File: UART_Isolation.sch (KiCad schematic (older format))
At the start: 8 parts

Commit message: Updated UART USB converter sheet, and isolation sheet
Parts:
- removed R905: 10k, Resistors_SMD:R_0603, symbol Custom-Library:R_Custom
- added U901: ISO7331C, Package_SO:SOIC-16W_7.5x10.3mm_P1.27mm, symbol Isolator:ISO7331C
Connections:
- net labels added: USB_DTR, USB_DTR_ISO
- net labels removed: ~USB_DTR, ~USB_DTR_ISO
- wire segments 34 -> 32
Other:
- note removed: "SWITCH TO DUAL SIGNAL ISOLATOR INSTEAD"
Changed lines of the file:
@@
 USB_UART_RX_ISO
 Text GLabel 7300 3700 2    60   Input ~ 0
-~USB_DTR_ISO
+USB_DTR_ISO
 $Comp
 L Custom-Library:GND_USB #PWR908
@@
 	4810 3900 4890 3900
 Connection ~ 4810 4000
-$Comp
-L Custom-Library:R_Custom R905
-U 1 1 5B330ED8
-P 6530 2940
-F 0 "R905" H 6470 2940 50  0000 R CNN
-F 1 "10k" V 6530 2940 50  0000 C CNN
-F 2 "Resistors_SMD:R_0603" H 6530 2940 50  0001 C CNN
-F 3 "" H 6530 2940 50  0001 C CNN
-F 4 "0603" H 6600 3020 50  0000 L CNN "display_footprint"
-F 5 "1%" H 6600 2940 50  0000 L CNN "Tolerance"
-F 6 "1/10W" H 6600 2870 50  0000 L CNN "Wattage"
-	1    6530 2940
-	1    0    0    1
-$EndComp
 Wire Wire Line
 	5690 3600 6220 3600
-Wire Wire Line
-	5690 3700 6530 3700
 Wire Wire Line
 	5690 3800 6860 3800
@@
 $EndComp
 Wire Wire Line
-	6530 3090 6530 3700
-Connection ~ 6530 3700
-Wire Wire Line
 	6860 3900 6860 3800
 Connection ~ 6860 3800
@@
 	1    0    0    -1
 $EndComp
-$Comp
-L Custom-Library:+5V_USB #PWR913
-U 1 1 5B334AE5
-P 6530 2790
-F 0 "#PWR913" H 6530 2640 50  0001 C CNN
-F 1 "+5V_USB" H 6530 2930 50  0000 C CNN
-F 2 "" H 6530 2790 50  0001 C CNN
-F 3 "" H 6530 2790 50  0001 C CNN
-	1    6530 2790
-	1    0    0    -1
-$EndComp
 Text GLabel 3280 3800 0    60   Input ~ 0
 USB_UART_TX
@@
 USB_UART_RX
 Text GLabel 3280 3700 0    60   Output ~ 0
-~USB_DTR
+USB_DTR
 $Comp
 L Custom-Library:R_Custom R902
@@
 	4810 4000 4810 4080
 Wire Wire Line
-	6530 3700 7300 3700
-Wire Wire Line
 	6860 3800 7300 3800
 Wire Wire Line
@@
 Wire Wire Line
 	4360 3600 4890 3600
-Text Notes 4480 1990 0    60   ~ 0
-SWITCH TO DUAL SIGNAL ISOLATOR INSTEAD
+Wire Wire Line
+	5690 3700 7300 3700
+$Comp
+L Isolator:ISO7331C U901
+U 1 1 5B50F39B
+P 5290 3700
+F 0 "U901" H 5040 4150 50  0000 C CNN
+F 1 "ISO7331C" H 5560 4150 50  0000 C CNN
+F 2 "Package_SO:SOIC-16W_7.5x10.3mm_P1.27mm" H 5290 3200 50  0001 C CIN
+F 3 "http://www.ti.com/lit/ds/symlink/iso7331c.pdf" H 5290 4100 50  0001 C CNN
+	1    5290 3700
+	-1   0    0    -1
+$EndComp
 $EndSCHEMATC

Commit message: Added a config field for every part, DNP some I2C pullups, added I2C header, changed some serial port functionality
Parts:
- removed R902: 10k, Resistors_SMD:R_0603, symbol Custom-Library:R_Custom
- added R? (x2): 10k, Resistors_SMD:R_0603, symbol Custom-Library:R_Custom
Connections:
- wire segments 32 -> 34
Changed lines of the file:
@@
 Comment4 ""
 $EndDescr
-Text GLabel 7300 3800 2    60   Output ~ 0
+Text GLabel 8000 3800 2    60   Output ~ 0
 USB_UART_TX_ISO
-Text GLabel 7300 3600 2    60   Input ~ 0
+Text GLabel 8000 3600 2    60   Input ~ 0
 USB_UART_RX_ISO
-Text GLabel 7300 3700 2    60   Input ~ 0
+Text GLabel 8000 3700 2    60   Input ~ 0
 USB_DTR_ISO
 $Comp
@@
 	1    0    0    -1
 $EndComp
-Text GLabel 3280 3800 0    60   Input ~ 0
+Text GLabel 2580 3800 0    60   Input ~ 0
 USB_UART_TX
-Text GLabel 3280 3600 0    60   Output ~ 0
+Text GLabel 2580 3600 0    60   Output ~ 0
 USB_UART_RX
-Text GLabel 3280 3700 0    60   Output ~ 0
+Text GLabel 2580 3700 0    60   Output ~ 0
 USB_DTR
-$Comp
-L Custom-Library:R_Custom R902
-U 1 1 5B334B6B
-P 4050 2940
-F 0 "R902" H 3990 2940 50  0000 R CNN
-F 1 "10k" V 4050 2940 50  0000 C CNN
-F 2 "Resistors_SMD:R_0603" H 4050 2940 50  0001 C CNN
-F 3 "" H 4050 2940 50  0001 C CNN
-F 4 "0603" H 4120 3020 50  0000 L CNN "display_footprint"
-F 5 "1%" H 4120 2940 50  0000 L CNN "Tolerance"
-F 6 "1/10W" H 4120 2870 50  0000 L CNN "Wattage"
-	1    4050 2940
-	-1   0    0    1
-$EndComp
-Wire Wire Line
-	3280 3600 4360 3600
-Wire Wire Line
-	3280 3700 4050 3700
-Wire Wire Line
-	3280 3800 3720 3800
 $Comp
 L Custom-Library:R_Custom R903
@@
 $EndComp
 Wire Wire Line
-	4050 3090 4050 3700
-Connection ~ 4050 3700
-Wire Wire Line
 	3720 3900 3720 3800
 Connection ~ 3720 3800
@@
 	4360 3900 4360 3600
 Connection ~ 4360 3600
-$Comp
-L Custom-Library:+3.3V #PWR902
-U 1 1 5B334D0F
-P 4050 2790
-F 0 "#PWR902" H 4050 2640 50  0001 C CNN
-F 1 "+3.3V" H 4050 2930 50  0000 C CNN
-F 2 "" H 4050 2790 50  0000 C CNN
-F 3 "" H 4050 2790 50  0000 C CNN
-	1    4050 2790
-	1    0    0    -1
-$EndComp
 $Comp
 L power:GND #PWR903
@@
 	4810 4000 4810 4080
 Wire Wire Line
-	6860 3800 7300 3800
-Wire Wire Line
-	6220 3600 7300 3600
-Wire Wire Line
 	6000 3400 6000 3500
 Wire Wire Line
 	4660 3400 4660 3500
 Wire Wire Line
-	4050 3700 4890 3700
-Wire Wire Line
 	3720 3800 4890 3800
 Wire Wire Line
 	4360 3600 4890 3600
-Wire Wire Line
-	5690 3700 7300 3700
 $Comp
 L Isolator:ISO7331C U901
@@
 	-1   0    0    -1
 $EndComp
+Wire Wire Line
+	6220 3600 8000 3600
+Wire Wire Line
+	6860 3800 8000 3800
+Wire Wire Line
+	5690 3700 7530 3700
+Wire Wire Line
+	2580 3600 4360 3600
+$Comp
+L Custom-Library:R_Custom R?
+U 1 1 5B51D46D
+P 3110 4050
+F 0 "R?" H 3050 4050 50  0000 R CNN
+F 1 "10k" V 3110 4050 50  0000 C CNN
+F 2 "Resistors_SMD:R_0603" H 3110 4050 50  0001 C CNN
+F 3 "" H 3110 4050 50  0001 C CNN
+F 4 "0603" H 3180 4130 50  0000 L CNN "display_footprint"
+F 5 "1%" H 3180 4050 50  0000 L CNN "Tolerance"
+F 6 "1/10W" H 3180 3980 50  0000 L CNN "Wattage"
+	1    3110 4050
+	-1   0    0    1
+$EndComp
+$Comp
+L power:GND #PWR?
+U 1 1 5B51D49E
+P 3110 4200
+F 0 "#PWR?" H 3110 3950 50  0001 C CNN
+F 1 "GND" H 3110 4050 50  0000 C CNN
+F 2 "" H 3110 4200 50  0001 C CNN
+F 3 "" H 3110 4200 50  0001 C CNN
+	1    3110 4200
+	1    0    0    -1
+$EndComp
+Wire Wire Line
+	3110 3900 3110 3700
+Wire Wire Line
+	2580 3800 3720 3800
+Wire Wire Line
+	2580 3700 3110 3700
+Connection ~ 3110 3700
+Wire Wire Line
+	3110 3700 4890 3700
+$Comp
+L Custom-Library:R_Custom R?
+U 1 1 5B51DA55
+P 7530 4050
+F 0 "R?" H 7470 4050 50  0000 R CNN
+F 1 "10k" V 7530 4050 50  0000 C CNN
+F 2 "Resistors_SMD:R_0603" H 7530 4050 50  0001 C CNN
+F 3 "" H 7530 4050 50  0001 C CNN
+F 4 "0603" H 7600 4130 50  0000 L CNN "display_footprint"
+F 5 "1%" H 7600 4050 50  0000 L CNN "Tolerance"
+F 6 "1/10W" H 7600 3980 50  0000 L CNN "Wattage"
+	1    7530 4050
+	1    0    0    1
+$EndComp
+$Comp
+L Custom-Library:GND_USB #PWR?
+U 1 1 5B51DA86
+P 7530 4200
+F 0 "#PWR?" H 7530 3950 50  0001 C CNN
+F 1 "GND_USB" H 7530 4050 50  0000 C CNN
+F 2 "" H 7530 4200 50  0001 C CNN
+F 3 "" H 7530 4200 50  0001 C CNN
+	1    7530 4200
+	1    0    0    -1
+$EndComp
+Wire Wire Line
+	7530 3900 7530 3700
+Connection ~ 7530 3700
+Wire Wire Line
+	7530 3700 8000 3700
 $EndSCHEMATC

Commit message: Annotated all components, finished assigning footprints, netlist generated
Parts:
- gave numbers to parts that had none: 2
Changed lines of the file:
@@
 USB_DTR_ISO
 $Comp
-L Custom-Library:GND_USB #PWR908
+L Custom-Library:GND_USB #PWR0908
 U 1 1 5B33B4C2
 P 5770 4080
-F 0 "#PWR908" H 5770 3830 50  0001 C CNN
+F 0 "#PWR0908" H 5770 3830 50  0001 C CNN
 F 1 "GND_USB" H 5770 3930 50  0000 C CNN
 F 2 "" H 5770 4080 50  0001 C CNN
@@
 Connection ~ 5770 4000
 $Comp
-L power:GND #PWR905
+L power:GND #PWR0905
 U 1 1 5B33B4E7
 P 4810 4080
-F 0 "#PWR905" H 4810 3830 50  0001 C CNN
+F 0 "#PWR0905" H 4810 3830 50  0001 C CNN
 F 1 "GND" H 4810 3930 50  0000 C CNN
 F 2 "" H 4810 4080 50  0001 C CNN
@@
 $EndComp
 $Comp
-L Custom-Library:GND_USB #PWR912
+L Custom-Library:GND_USB #PWR0912
 U 1 1 5B3334DB
 P 6220 4200
-F 0 "#PWR912" H 6220 3950 50  0001 C CNN
+F 0 "#PWR0912" H 6220 3950 50  0001 C CNN
 F 1 "GND_USB" H 6220 4050 50  0000 C CNN
 F 2 "" H 6220 4200 50  0001 C CNN
@@
 $EndComp
 $Comp
-L Custom-Library:GND_USB #PWR914
+L Custom-Library:GND_USB #PWR0914
 U 1 1 5B3334F2
 P 6860 4200
-F 0 "#PWR914" H 6860 3950 50  0001 C CNN
+F 0 "#PWR0914" H 6860 3950 50  0001 C CNN
 F 1 "GND_USB" H 6860 4050 50  0000 C CNN
 F 2 "" H 6860 4200 50  0001 C CNN
@@
 $EndComp
 $Comp
-L power:GND #PWR907
+L power:GND #PWR0907
 U 1 1 5B333B49
 P 4830 4900
-F 0 "#PWR907" H 4830 4650 50  0001 C CNN
+F 0 "#PWR0907" H 4830 4650 50  0001 C CNN
 F 1 "GND" H 4830 4750 50  0000 C CNN
 F 2 "" H 4830 4900 50  0001 C CNN
@@
 $EndComp
 $Comp
-L Custom-Library:GND_USB #PWR910
+L Custom-Library:GND_USB #PWR0910
 U 1 1 5B333B66
 P 5940 4900
-F 0 "#PWR910" H 5940 4650 50  0001 C CNN
+F 0 "#PWR0910" H 5940 4650 50  0001 C CNN
 F 1 "GND_USB" H 5940 4750 50  0000 C CNN
 F 2 "" H 5940 4900 50  0001 C CNN
@@
 $EndComp
 $Comp
-L Custom-Library:+5V_USB #PWR911
+L Custom-Library:+5V_USB #PWR0911
 U 1 1 5B333B91
 P 6000 3320
-F 0 "#PWR911" H 6000 3170 50  0001 C CNN
+F 0 "#PWR0911" H 6000 3170 50  0001 C CNN
 F 1 "+5V_USB" H 6000 3460 50  0000 C CNN
 F 2 "" H 6000 3320 50  0001 C CNN
@@
 Connection ~ 6000 3400
 $Comp
-L Custom-Library:+3.3V #PWR904
+L Custom-Library:+3.3V #PWR0904
 U 1 1 5B334082
 P 4660 3320
-F 0 "#PWR904" H 4660 3170 50  0001 C CNN
+F 0 "#PWR0904" H 4660 3170 50  0001 C CNN
 F 1 "+3.3V" H 4660 3460 50  0000 C CNN
 F 2 "" H 4660 3320 50  0000 C CNN
@@
 Connection ~ 4660 3400
 $Comp
-L Custom-Library:+5V_USB #PWR909
+L Custom-Library:+5V_USB #PWR0909
 U 1 1 5B33458B
 P 5940 4600
-F 0 "#PWR909" H 5940 4450 50  0001 C CNN
+F 0 "#PWR0909" H 5940 4450 50  0001 C CNN
 F 1 "+5V_USB" H 5940 4740 50  0000 C CNN
 F 2 "" H 5940 4600 50  0001 C CNN
@@
 $EndComp
 $Comp
-L Custom-Library:+3.3V #PWR906
+L Custom-Library:+3.3V #PWR0906
 U 1 1 5B3345D2
 P 4830 4600
-F 0 "#PWR906" H 4830 4450 50  0001 C CNN
+F 0 "#PWR0906" H 4830 4450 50  0001 C CNN
 F 1 "+3.3V" H 4830 4740 50  0000 C CNN
 F 2 "" H 4830 4600 50  0000 C CNN
@@
 Connection ~ 4360 3600
 $Comp
-L power:GND #PWR903
+L power:GND #PWR0903
 U 1 1 5B334D88
 P 4360 4200
-F 0 "#PWR903" H 4360 3950 50  0001 C CNN
+F 0 "#PWR0903" H 4360 3950 50  0001 C CNN
 F 1 "GND" H 4360 4050 50  0000 C CNN
 F 2 "" H 4360 4200 50  0001 C CNN
@@
 $EndComp
 $Comp
-L power:GND #PWR901
+L power:GND #PWR0901
 U 1 1 5B33526C
 P 3720 4200
-F 0 "#PWR901" H 3720 3950 50  0001 C CNN
+F 0 "#PWR0901" H 3720 3950 50  0001 C CNN
 F 1 "GND" H 3720 4050 50  0000 C CNN
 F 2 "" H 3720 4200 50  0001 C CNN
@@
 	2580 3600 4360 3600
 $Comp
-L Custom-Library:R_Custom R?
+L Custom-Library:R_Custom R902
 U 1 1 5B51D46D
 P 3110 4050
-F 0 "R?" H 3050 4050 50  0000 R CNN
+F 0 "R902" H 3050 4050 50  0000 R CNN
 F 1 "10k" V 3110 4050 50  0000 C CNN
 F 2 "Resistors_SMD:R_0603" H 3110 4050 50  0001 C CNN
@@
 $EndComp
 $Comp
-L power:GND #PWR?
+L power:GND #PWR0902
 U 1 1 5B51D49E
 P 3110 4200
-F 0 "#PWR?" H 3110 3950 50  0001 C CNN
+F 0 "#PWR0902" H 3110 3950 50  0001 C CNN
 F 1 "GND" H 3110 4050 50  0000 C CNN
 F 2 "" H 3110 4200 50  0001 C CNN
@@
 	3110 3700 4890 3700
 $Comp
-L Custom-Library:R_Custom R?
+L Custom-Library:R_Custom R905
 U 1 1 5B51DA55
 P 7530 4050
-F 0 "R?" H 7470 4050 50  0000 R CNN
+F 0 "R905" H 7470 4050 50  0000 R CNN
 F 1 "10k" V 7530 4050 50  0000 C CNN
 F 2 "Resistors_SMD:R_0603" H 7530 4050 50  0001 C CNN
@@
 $EndComp
 $Comp
-L Custom-Library:GND_USB #PWR?
+L Custom-Library:GND_USB #PWR0913
 U 1 1 5B51DA86
 P 7530 4200
-F 0 "#PWR?" H 7530 3950 50  0001 C CNN
+F 0 "#PWR0913" H 7530 3950 50  0001 C CNN
 F 1 "GND_USB" H 7530 4050 50  0000 C CNN
 F 2 "" H 7530 4200 50  0001 C CNN

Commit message: Changed POS3P3 MOSFETs, further schematic enhancements, footprint updates, and arranged a few more pages of components on PCB
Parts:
- U901: footprint Package_SO:SOIC-16W_7.5x10.3mm_P1.27mm -> Housings_SOIC:SOIC-16W_7.5x10.3mm_Pitch1.27mm; Digi-Key PN (none) -> 296-47261-1-ND
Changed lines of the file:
@@
 F 0 "U901" H 5040 4150 50  0000 C CNN
 F 1 "ISO7331C" H 5560 4150 50  0000 C CNN
-F 2 "Package_SO:SOIC-16W_7.5x10.3mm_P1.27mm" H 5290 3200 50  0001 C CIN
+F 2 "Housings_SOIC:SOIC-16W_7.5x10.3mm_Pitch1.27mm" H 5290 3200 50  0001 C CIN
 F 3 "http://www.ti.com/lit/ds/symlink/iso7331c.pdf" H 5290 4100 50  0001 C CNN
+F 4 "296-47261-1-ND" H 5290 3700 50  0001 C CNN "Digi-Key PN"
 	1    5290 3700
 	-1   0    0    -1

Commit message: Arranged USB components, various footprint fixes, added GND_USB EMI cap
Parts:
- added C903: 22000pF, Capacitors_SMD:C_2220, symbol Custom-Library:C_Custom
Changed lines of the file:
@@
 Wire Wire Line
 	7530 3700 8000 3700
+$Comp
+L Custom-Library:C_Custom C?
+U 1 1 5B585E45
+P 5290 5320
+AR Path="/5A0A3EA5/5B585E45" Ref="C?"  Part="1"
+AR Path="/5A0B00BA/5B585E45" Ref="C?"  Part="1"
+AR Path="/5A19B2DB/5B585E45" Ref="C903"  Part="1"
+F 0 "C903" V 5450 5320 50  0000 C CNN
+F 1 "22000pF" V 5541 5320 50  0000 C CNN
+F 2 "Capacitors_SMD:C_2220" H 5328 5170 50  0001 C CNN
+F 3 "" H 5315 5420 50  0001 C CNN
+F 4 "2220" V 5632 5320 50  0000 C CNN "display_footprint"
+F 5 "250VAC" V 5723 5320 50  0000 C CNN "Voltage"
+F 6 "X7R" V 5814 5320 50  0000 C CNN "Dielectric"
+F 7 "720-1587-1-ND" V 5290 5320 50  0001 C CNN "Digi-Key PN"
+	1    5290 5320
+	0    1    1    0
+$EndComp
+$Comp
+L Custom-Library:GND_USB #PWR0103
+U 1 1 5B58639E
+P 5440 5320
+F 0 "#PWR0103" H 5440 5070 50  0001 C CNN
+F 1 "GND_USB" H 5440 5170 50  0000 C CNN
+F 2 "" H 5440 5320 50  0001 C CNN
+F 3 "" H 5440 5320 50  0001 C CNN
+	1    5440 5320
+	0    -1   -1   0
+$EndComp
+$Comp
+L power:GND #PWR0104
+U 1 1 5B5863DB
+P 5140 5320
+F 0 "#PWR0104" H 5140 5070 50  0001 C CNN
+F 1 "GND" H 5140 5170 50  0000 C CNN
+F 2 "" H 5140 5320 50  0001 C CNN
+F 3 "" H 5140 5320 50  0001 C CNN
+	1    5140 5320
+	0    1    1    0
+$EndComp
 $EndSCHEMATC

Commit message: Added a bunch of Digi-Key PN's
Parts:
- C901, C902: Digi-Key PN (none) -> 399-6856-1-ND
- R901, R902, R903, R904, R905, R906: Digi-Key PN (none) -> 541-10.0KHCT-ND
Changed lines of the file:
@@
 F 5 "1%" H 6290 4050 50  0000 L CNN "Tolerance"
 F 6 "1/10W" H 6290 3980 50  0000 L CNN "Wattage"
+F 7 "541-10.0KHCT-ND" H 0   0   50  0001 C CNN "Digi-Key PN"
 	1    6220 4050
 	1    0    0    1
@@
 F 5 "1%" H 6930 4050 50  0000 L CNN "Tolerance"
 F 6 "1/10W" H 6930 3980 50  0000 L CNN "Wattage"
+F 7 "541-10.0KHCT-ND" H 0   0   50  0001 C CNN "Digi-Key PN"
 	1    6860 4050
 	1    0    0    1
@@
 F 5 "50V" H 5790 4750 50  0000 R CNN "Voltage"
 F 6 "X7R" H 5790 4650 50  0000 R CNN "Dielectric"
+F 7 "399-6856-1-ND" H 0   0   50  0001 C CNN "Digi-Key PN"
 	1    5940 4750
 	1    0    0    -1
@@
 F 5 "50V" H 4680 4750 50  0000 R CNN "Voltage"
 F 6 "X7R" H 4680 4650 50  0000 R CNN "Dielectric"
+F 7 "399-6856-1-ND" H 0   0   50  0001 C CNN "Digi-Key PN"
 	1    4830 4750
 	1    0    0    -1
@@
 F 5 "1%" H 4430 4050 50  0000 L CNN "Tolerance"
 F 6 "1/10W" H 4430 3980 50  0000 L CNN "Wattage"
+F 7 "541-10.0KHCT-ND" H 0   0   50  0001 C CNN "Digi-Key PN"
 	1    4360 4050
 	-1   0    0    1
@@
 F 5 "1%" H 3790 4050 50  0000 L CNN "Tolerance"
 F 6 "1/10W" H 3790 3980 50  0000 L CNN "Wattage"
+F 7 "541-10.0KHCT-ND" H 0   0   50  0001 C CNN "Digi-Key PN"
 	1    3720 4050
 	-1   0    0    1
@@
 F 5 "1%" H 3180 4050 50  0000 L CNN "Tolerance"
 F 6 "1/10W" H 3180 3980 50  0000 L CNN "Wattage"
+F 7 "541-10.0KHCT-ND" H 0   0   50  0001 C CNN "Digi-Key PN"
 	1    3110 4050
 	-1   0    0    1
@@
 F 5 "1%" H 7600 4050 50  0000 L CNN "Tolerance"
 F 6 "1/10W" H 7600 3980 50  0000 L CNN "Wattage"
+F 7 "541-10.0KHCT-ND" H 0   0   50  0001 C CNN "Digi-Key PN"
 	1    7530 4050
 	1    0    0    1

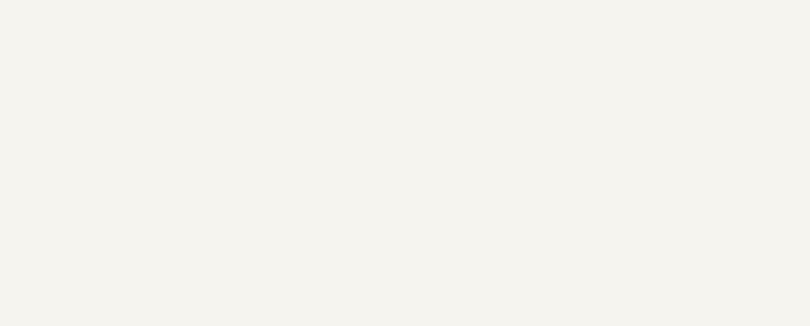
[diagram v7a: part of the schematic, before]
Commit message: Arranged more components on PCB, cleaned up schematic, added page titles, finished finding DigiKey PN's
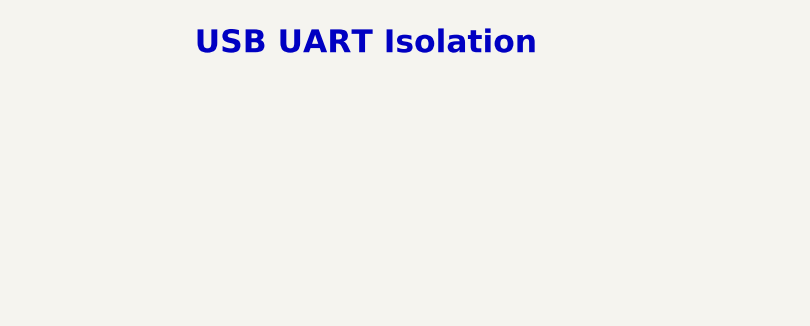
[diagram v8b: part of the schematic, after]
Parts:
- R901, R902, R903, R904, R905, R906: Digi-Key PN 541-10.0KHCT-ND -> P10.0KHCT-ND
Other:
- note added: "USB UART Isolation"
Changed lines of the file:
@@
 F 5 "1%" H 6290 4050 50  0000 L CNN "Tolerance"
 F 6 "1/10W" H 6290 3980 50  0000 L CNN "Wattage"
-F 7 "541-10.0KHCT-ND" H 0   0   50  0001 C CNN "Digi-Key PN"
+F 7 "P10.0KHCT-ND" H 0   0   50  0001 C CNN "Digi-Key PN"
 	1    6220 4050
 	1    0    0    1
@@
 F 5 "1%" H 6930 4050 50  0000 L CNN "Tolerance"
 F 6 "1/10W" H 6930 3980 50  0000 L CNN "Wattage"
-F 7 "541-10.0KHCT-ND" H 0   0   50  0001 C CNN "Digi-Key PN"
+F 7 "P10.0KHCT-ND" H 0   0   50  0001 C CNN "Digi-Key PN"
 	1    6860 4050
 	1    0    0    1
@@
 F 5 "1%" H 4430 4050 50  0000 L CNN "Tolerance"
 F 6 "1/10W" H 4430 3980 50  0000 L CNN "Wattage"
-F 7 "541-10.0KHCT-ND" H 0   0   50  0001 C CNN "Digi-Key PN"
+F 7 "P10.0KHCT-ND" H 0   0   50  0001 C CNN "Digi-Key PN"
 	1    4360 4050
 	-1   0    0    1
@@
 F 5 "1%" H 3790 4050 50  0000 L CNN "Tolerance"
 F 6 "1/10W" H 3790 3980 50  0000 L CNN "Wattage"
-F 7 "541-10.0KHCT-ND" H 0   0   50  0001 C CNN "Digi-Key PN"
+F 7 "P10.0KHCT-ND" H 0   0   50  0001 C CNN "Digi-Key PN"
 	1    3720 4050
 	-1   0    0    1
@@
 F 5 "1%" H 3180 4050 50  0000 L CNN "Tolerance"
 F 6 "1/10W" H 3180 3980 50  0000 L CNN "Wattage"
-F 7 "541-10.0KHCT-ND" H 0   0   50  0001 C CNN "Digi-Key PN"
+F 7 "P10.0KHCT-ND" H 0   0   50  0001 C CNN "Digi-Key PN"
 	1    3110 4050
 	-1   0    0    1
@@
 F 5 "1%" H 7600 4050 50  0000 L CNN "Tolerance"
 F 6 "1/10W" H 7600 3980 50  0000 L CNN "Wattage"
-F 7 "541-10.0KHCT-ND" H 0   0   50  0001 C CNN "Digi-Key PN"
+F 7 "P10.0KHCT-ND" H 0   0   50  0001 C CNN "Digi-Key PN"
 	1    7530 4050
 	1    0    0    1
@@
 	0    1    1    0
 $EndComp
+Text Notes 4610 1130 0    100  ~ 20
+USB UART Isolation
 $EndSCHEMATC
